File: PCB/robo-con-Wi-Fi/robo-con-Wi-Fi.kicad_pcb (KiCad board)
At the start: 4 copper layers, 86 x 67 mm, 119 parts, among them J1 Conn_01x04, J2 SMA-J, J3 Conn_01x05, J4 Conn_01x01, J5 Conn_01x02, J6 Conn_01x01, J7 Conn_01x06, Q1 2SC3325-Y, SW1 SW_Push, SW2 SW_Push, U1 STM32H723VGTx, U10 MCP73831-2-OT, U11 LM66100DCK, U12 NJM12877, U13 TXB0606DYYR, U14 TPS628513DRLR, U15 LM66100DCK, U18 USB_Type-C, U2 LBEE5HY2FY, U3 TXU0204, U5 RKJXV122400R, U6 IS25LP064D-JLLE, U7 RKJXV122400R, U8 TMHU28, U9 TMHU28, Y2 XRCGB25M000FFS1AR0

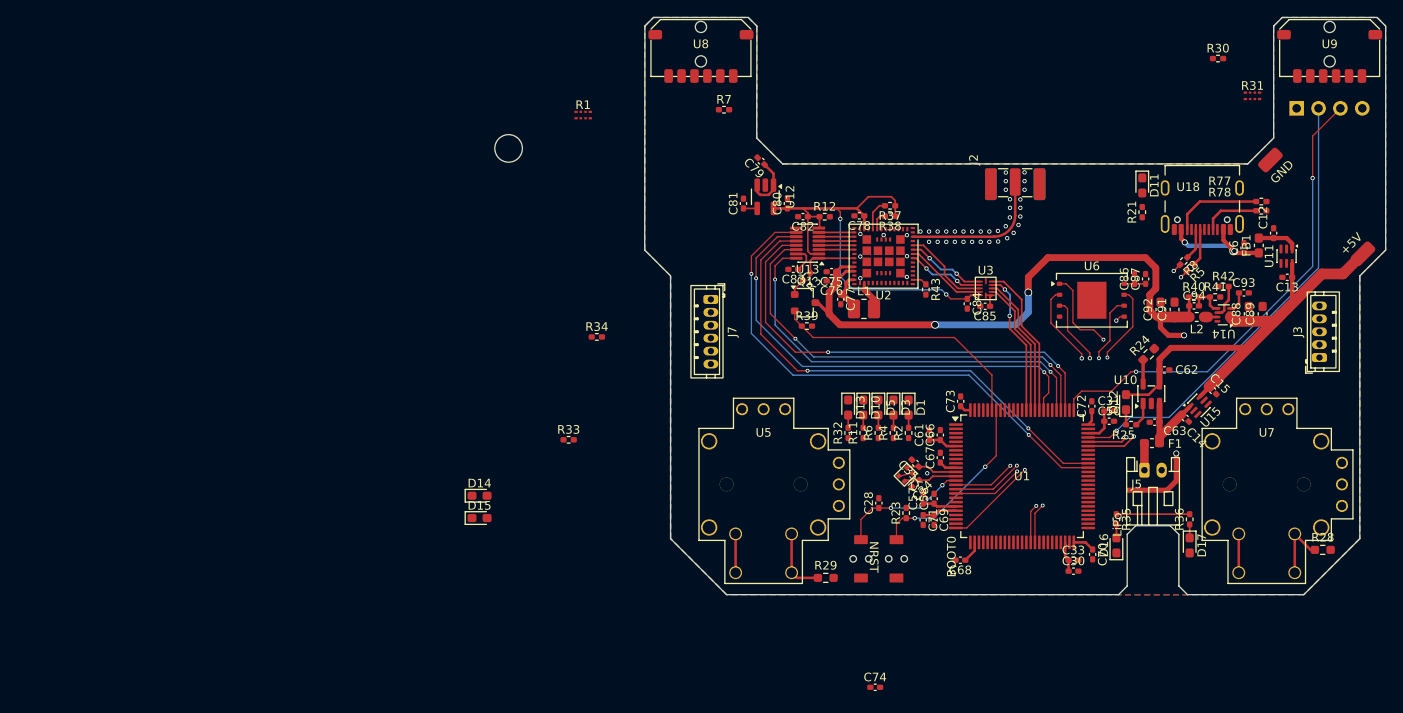
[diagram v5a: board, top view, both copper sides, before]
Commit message: フットプリントを配置残り配線と配線長合わせ
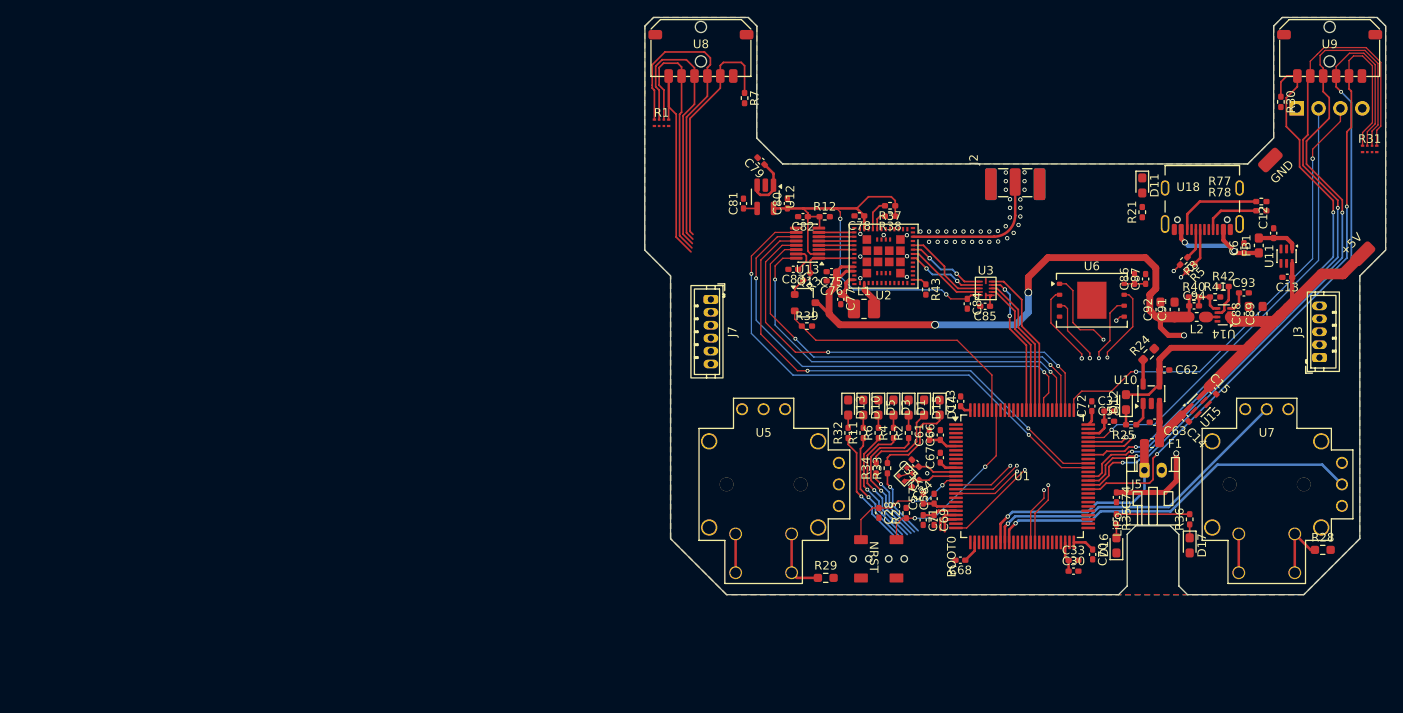
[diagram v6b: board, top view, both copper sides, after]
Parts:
- removed H2: MountingHole, MountingHole:MountingHole_3.2mm_M3
- moved D14 54.4 mm to (161.2, 68.3), turned to -90 degrees
- moved D15 53.2 mm to (159.4, 68.3), turned to -90 degrees
- moved R33 37.1 mm to (155.2, 75.3), turned to 90 degrees
- moved R34 35.8 mm to (153.9, 75.3), turned to 90 degrees
- moved C74 35.6 mm to (181.8, 78.7), turned to -90 degrees
- moved R31 14.9 mm to (211.1, 38.3)
- moved R1 9.14 mm to (128.9, 35.2)
- moved R30 8.86 mm to (200.8, 32.8), turned to -90 degrees
- moved R7 2.74 mm to (138.6, 32.4), turned to -90 degrees
- moved C28 1.13 mm to (154.2, 80.5), turned to -90 degrees
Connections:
- U1 pad 33: unconnected-(U1-PC5-Pad33) -> LiPo_Observer
- U1 pad 34: unconnected-(U1-PB0-Pad34) -> Right_X_Stick
- U1 pad 35: unconnected-(U1-PB1-Pad35) -> Right_Y_Stick
- U1 pad 60: unconnected-(U1-PD13-Pad60) -> Right_Lever_Switch_4
- U1 pad 61: unconnected-(U1-PD14-Pad61) -> Right_Lever_Switch_3
- U1 pad 62: unconnected-(U1-PD15-Pad62) -> Right_Lever_Switch_0
- U1 pad 63: unconnected-(U1-PC6-Pad63) -> Right_Lever_Switch_2
- U1 pad 68: unconnected-(U1-PA9-Pad68) -> Right_Lever_Switch_1
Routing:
- net Right_Lever_Switch_0: track 0.00 -> 85.0 mm, vias 0 -> 2
- net Right_Lever_Switch_2: track 0.00 -> 84.3 mm, vias 0 -> 2
- net Right_Lever_Switch_4: track 0.00 -> 81.7 mm, vias 0 -> 2
- net Right_Lever_Switch_3: track 0.00 -> 77.9 mm, vias 0 -> 2
- net Right_Lever_Switch_1: track 0.00 -> 65.7 mm, vias 0 -> 2
- net Right_Y_Stick: track 0.00 -> 44.2 mm, vias 0 -> 1
- net Right_X_Stick: track 0.00 -> 37.9 mm, vias 0 -> 1
- net Left_Lever_Switch_4: track 0.00 -> 36.6 mm
- net Left_Lever_Switch_0: track 0.00 -> 32.9 mm
- net Left_Lever_Switch_2: track 0.00 -> 30.9 mm
- net Left_Lever_Switch_3: track 0.00 -> 27.5 mm
- net Left_Lever_Switch_1: track 0.00 -> 26.5 mm
- net LiPo_Observer: track 3.14 -> 26.0 mm, vias 0 -> 1
- net LED_0: track 0.00 -> 16.5 mm, vias 0 -> 1
- net LED_1: track 0.00 -> 15.2 mm, vias 0 -> 1
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
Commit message: PCB配線した　長さ合わせた後確認
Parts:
- moved J7 71.4 mm to (205.3, 65.9), turned to 90 degrees
- moved J3 70.7 mm to (134.7, 59.1), turned to -90 degrees
- moved R24 0.66 mm to (184.9, 62.0), turned to 90 degrees
- moved C73 0.17 mm to (163.8, 67.4)
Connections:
- U1 pad 1: unconnected-(U1-PE2-Pad1) -> Left_Lever_Switch_1
- U1 pad 2: unconnected-(U1-PE3-Pad2) -> Left_Lever_Switch_2
- U1 pad 22: unconnected-(U1-PA0-Pad22) -> Left_Y_Stick
- U1 pad 23: unconnected-(U1-PA1-Pad23) -> Left_X_Stick
- U1 pad 28: unconnected-(U1-PA4-Pad28) -> LED_USB
- U1 pad 29: unconnected-(U1-PA5-Pad29) -> LED_Wi-Fi
- U1 pad 3: unconnected-(U1-PE4-Pad3) -> Left_Lever_Switch_0
- U1 pad 30: unconnected-(U1-PA6-Pad30) -> LED_0
- U1 pad 31: unconnected-(U1-PA7-Pad31) -> LED_1
- U1 pad 32: unconnected-(U1-PC4-Pad32) -> LED_2
- U1 pad 36: unconnected-(U1-PB2-Pad36) -> LED_3
- U1 pad 37: unconnected-(U1-PE7-Pad37) -> LED_4
- U1 pad 38: unconnected-(U1-PE8-Pad38) -> Right_Push_Stick
- U1 pad 4: unconnected-(U1-PE5-Pad4) -> Left_Lever_Switch_4
- U1 pad 43: unconnected-(U1-PE13-Pad43) -> Right_Button_5
- U1 pad 44: unconnected-(U1-PE14-Pad44) -> Right_Button_6
- U1 pad 45: unconnected-(U1-PE15-Pad45) -> Right_Button_7
- U1 pad 46: unconnected-(U1-PB10-Pad46) -> Left_Push_Stick
- U1 pad 47: unconnected-(U1-PB11-Pad47) -> LiPo_State
- U1 pad 5: unconnected-(U1-PE6-Pad5) -> Left_Lever_Switch_3
- U1 pad 51: unconnected-(U1-PB12-Pad51) -> Left_Button_1
- U1 pad 52: unconnected-(U1-PB13-Pad52) -> Left_Button_2
- U1 pad 53: unconnected-(U1-PB14-Pad53) -> Left_Button_3
- U1 pad 54: unconnected-(U1-PB15-Pad54) -> Left_Button_4
- U1 pad 92: unconnected-(U1-PB6-Pad92) -> BT_ON
- U1 pad 93: unconnected-(U1-PB7-Pad93) -> WL_ON
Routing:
- net +3.3V: track 146.3 -> 460.4 mm, vias 4 -> 16
- net Right_Button_5: track 0.00 -> 58.6 mm, vias 0 -> 1
- net Right_Button_6: track 0.00 -> 58.3 mm, vias 0 -> 1
- net Right_Button_7: track 0.00 -> 58.0 mm, vias 0 -> 1
- net Left_Lever_Switch_3: track 27.5 -> 78.5 mm, vias 0 -> 2
- net Left_Lever_Switch_4: track 36.6 -> 86.0 mm, vias 0 -> 2
- net Left_Lever_Switch_0: track 32.9 -> 81.3 mm, vias 0 -> 2
- net Left_Lever_Switch_2: track 30.9 -> 78.0 mm, vias 0 -> 2
- net Right_Push_Stick: track 7.60 -> 54.1 mm, vias 0 -> 1
- net Left_Lever_Switch_1: track 26.5 -> 70.8 mm, vias 0 -> 2
- net Left_Button_4: track 0.00 -> 39.5 mm, vias 0 -> 1
- net Left_X_Stick: track 0.00 -> 39.4 mm
- net Left_Button_3: track 0.00 -> 39.1 mm, vias 0 -> 1
- net Left_Button_2: track 0.00 -> 38.7 mm, vias 0 -> 1
- net Left_Button_1: track 0.00 -> 38.2 mm, vias 0 -> 1
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
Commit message: ほぼ完成
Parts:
- added G***: LOGO, LOGO, F.Cu at (132.6, 47.6)
- added R26: 1k, Resistor_SMD:R_0603_1608Metric_Pad0.98x0.95mm_HandSolder, B.Cu at (177.7, 78.1)
- added R27: 1k, Resistor_SMD:R_0603_1608Metric_Pad0.98x0.95mm_HandSolder, B.Cu at (182.3, 75.8)
- moved C82 0.14 mm to (145.2, 46.1)
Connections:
- F1 pad 1: LiPo_Observer -> Net-(J5-Pin_1)
- J5 pad 1: LiPo_Observer -> Net-(J5-Pin_1)
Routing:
- net LiPo_Observer: track 24.6 -> 17.7 mm
- net Net-(J5-Pin_1): track 0.00 -> 5.02 mm
- net SWDIO: track 52.9 -> 56.1 mm
- net BT_ON: track 33.1 -> 35.3 mm
- net WL_ON: track 36.3 -> 38.0 mm
- net +3.3V: track 460.4 -> 459.6 mm
- net NRST: track 98.1 -> 98.8 mm
- net GND: vias 124 -> 535
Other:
- board text added: "Bad"
- board text added: "C1"
- board text added: "C3"
- board text added: "C6.5"
- board text added: "Good"
- board text added: "LED0"
- board text added: "LED1"
- board text added: "LED2"
- board text added: "LED3"
- board text added: "LED4"
- board text added: "LEDUSB"
- board text added: "LEDWL"
- board text added: "Robo-Con-Type-Wi-Fi6E"
- board text added: "State"
